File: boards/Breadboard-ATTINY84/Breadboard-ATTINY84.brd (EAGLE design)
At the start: 15.2 x 27.9 mm, 8 parts, among them J1 PINHD-1X7, J2 PINHD-1X7, U1 ATTINY84-20PU

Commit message: Updated breadboard ATTiny84
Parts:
- added D2: LED-0805, SaintGimp:LED-0805
- added R3: 330R, SaintGimp:RESISTOR-0805
- D1: value LED -> LED-0805; device SaintGimp:LED5MM -> SaintGimp:LED-0805
- moved D1 2.84 mm to (8.89, 25.4)
- moved R1 1.90 mm to (8.89, 21.0), flipped to the top, turned to 90 degrees
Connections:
- removed net N$5: J1.5, U1.5
- new net LED: J1.5, R3.1, U1.5
- new net N$1: D2.1, R3.2
- net GND: now also D1.2, D2.2; no longer D1.K
- net N$7: now also D1.1; no longer D1.A
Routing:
- net LED: track 0.00 -> 20.6 mm, vias 0 -> 1
- net GND: track 0.00 -> 4.03 mm, vias 0 -> 1
- net MISO: track 29.1 -> 25.5 mm
- net N$7: track 5.45 -> 2.45 mm
- net N$5: track 2.54 -> 0.00 mm
- net N$1: track 0.00 -> 2.45 mm
- net VCC: track 16.6 -> 19.0 mm, vias 0 -> 1
- net SCK: track 27.0 -> 26.2 mm
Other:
- board text added: "PIN5"
- board text added: "PWR"
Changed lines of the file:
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@@
 <layer number="112" name="tSilk" color="7" fill="1" visible="yes" active="yes"/>
 <layer number="113" name="IDFDebug" color="7" fill="1" visible="yes" active="yes"/>
+<layer number="114" name="FRNTMAAT1" color="7" fill="1" visible="yes" active="yes"/>
+<layer number="115" name="FRNTMAAT2" color="7" fill="1" visible="yes" active="yes"/>
 <layer number="116" name="Patch_BOT" color="9" fill="4" visible="yes" active="yes"/>
+<layer number="117" name="BACKMAAT1" color="7" fill="1" visible="yes" active="yes"/>
 <layer number="118" name="Rect_Pads" color="7" fill="1" visible="no" active="no"/>
+<layer number="119" name="KAP_TEKEN" color="7" fill="1" visible="yes" active="yes"/>
+<layer number="120" name="KAP_MAAT1" color="7" fill="1" visible="yes" active="yes"/>
 <layer number="121" name="_tsilk" color="7" fill="1" visible="yes" active="yes"/>
 <layer number="122" name="_bsilk" color="7" fill="1" visible="yes" active="yes"/>
@@
 <layer number="128" name="_bValues" color="7" fill="1" visible="yes" active="yes"/>
 <layer number="129" name="Mask" color="7" fill="1" visible="yes" active="yes"/>
+<layer number="130" name="SMDSTROOK" color="7" fill="1" visible="yes" active="yes"/>
 <layer number="131" name="tAdjust" color="7" fill="1" visible="no" active="yes"/>
 <layer number="132" name="bAdjust" color="7" fill="1" visible="no" active="yes"/>
@@
 <text x="5.715" y="1.27" size="1.016" layer="122" rot="MR90">v1.1</text>
 <text x="6.985" y="1.27" size="1.016" layer="122" rot="MR90">ATTiny84</text>
+<circle x="5.842" y="19.304" radius="0.359209375" width="0.6096" layer="121"/>
+<text x="7.62" y="24.13" size="0.8128" layer="121" rot="R90">PWR</text>
+<text x="14.605" y="24.13" size="0.8128" layer="121" rot="R90">PIN5</text>
 </plain>
 <attributes>
@@
 </class>
 </classes>
-<designrules name="Saintgimp-OSHPark">
+<designrules name="Saintgimp-OSHPark *">
 <description language="de">&lt;b&gt;EAGLE Design Rules&lt;/b&gt;
 &lt;p&gt;
@@
 <param name="msMicroVia" value="13mil"/>
 <param name="msBlindViaRatio" value="0.5"/>
-<param name="rvPadTop" value="0.4"/>
+<param name="rvPadTop" value="0.35"/>
 <param name="rvPadInner" value="0.25"/>
-<param name="rvPadBottom" value="0.4"/>
+<param name="rvPadBottom" value="0.35"/>
 <param name="rvViaOuter" value="0.25"/>
 <param name="rvViaInner" value="0.25"/>
@@
 <attribute name="NAME" x="10.287" y="16.3195" size="0.8128" layer="26" rot="MR0"/>
 </element>
-<element name="D1" library="SaintGimp" package="LED5MM" value="LED" x="11.43" y="24.13" smashed="yes" rot="R90">
-<attribute name="NAME" x="13.4366" y="20.32" size="0.8128" layer="25" ratio="10"/>
-</element>
-<element name="R1" library="SaintGimp" package="RESISTOR-0805" value="330R" x="8.89" y="19.05" smashed="yes" rot="MR180">
-<attribute name="NAME" x="10.668" y="19.2405" size="0.8128" layer="26" rot="MR180"/>
+<element name="D1" library="SaintGimp" package="LED-0805" value="LED-0805" x="8.89" y="25.4" smashed="yes" rot="R90"/>
+<element name="R1" library="SaintGimp" package="RESISTOR-0805" value="330R" x="8.89" y="20.955" smashed="yes" rot="R90">
+<attribute name="NAME" x="7.8105" y="20.193" size="0.8128" layer="25" rot="R90"/>
 </element>
 <element name="R2" library="SaintGimp" package="RESISTOR-0805" value="10K" x="6.35" y="12.7" smashed="yes" rot="MR90">
@@
 <element name="J1" library="SaintGimp" package="1X07" value="PINHD-1X7" x="1.27" y="8.89" smashed="yes" rot="MR270"/>
 <element name="J2" library="SaintGimp" package="1X07" value="PINHD-1X7" x="13.97" y="8.89" smashed="yes" rot="MR90"/>
+<element name="R3" library="SaintGimp" package="RESISTOR-0805" value="330R" x="12.7" y="20.955" smashed="yes" rot="R90">
+<attribute name="NAME" x="11.6205" y="20.193" size="0.8128" layer="25" rot="R90"/>
+</element>
+<element name="D2" library="SaintGimp" package="LED-0805" value="LED-0805" x="12.7" y="25.4" smashed="yes" rot="R90"/>
 </elements>
 <signals>
@@
 <contactref element="ISP1" pad="6"/>
 <contactref element="C1" pad="1"/>
-<contactref element="D1" pad="K"/>
+<contactref element="D1" pad="2"/>
 <contactref element="U1" pad="14"/>
 <contactref element="J2" pad="7"/>
+<via x="10.795" y="26.67" extent="1-16" drill="0.5"/>
+<wire x1="8.89" y1="26.4" x2="9.16" y2="26.67" width="0.254" layer="1"/>
+<wire x1="9.16" y1="26.67" x2="10.795" y2="26.67" width="0.254" layer="1"/>
+<contactref element="D2" pad="2"/>
+<wire x1="12.7" y1="26.4" x2="12.43" y2="26.67" width="0.254" layer="1"/>
+<wire x1="12.43" y1="26.67" x2="10.795" y2="26.67" width="0.254" layer="1"/>
 </signal>
 <signal name="MISO">
@@
 <contactref element="U1" pad="8"/>
 <contactref element="J2" pad="1"/>
-<wire x1="5.08" y1="21.59" x2="5.08" y2="20.955" width="0.254" layer="1"/>
-<wire x1="5.08" y1="20.955" x2="6.35" y2="22.225" width="0.254" layer="1"/>
-<wire x1="6.35" y1="22.225" x2="8.255" y2="22.225" width="0.254" layer="1"/>
-<wire x1="8.255" y1="22.225" x2="9.525" y2="20.955" width="0.254" layer="1"/>
-<wire x1="9.525" y1="20.955" x2="9.525" y2="3.175" width="0.254" layer="1"/>
-<wire x1="9.525" y1="3.175" x2="11.43" y2="1.27" width="0.254" layer="1"/>
 <wire x1="11.43" y1="1.27" x2="13.97" y2="1.27" width="0.254" layer="1"/>
+<wire x1="5.08" y1="21.59" x2="5.715" y2="20.955" width="0.254" layer="1"/>
+<wire x1="5.715" y1="20.955" x2="5.715" y2="6.985" width="0.254" layer="1"/>
+<wire x1="5.715" y1="6.985" x2="11.43" y2="1.27" width="0.254" layer="1"/>
 </signal>
 <signal name="SCK">
@@
 <contactref element="U1" pad="9"/>
 <contactref element="J2" pad="2"/>
-<wire x1="10.16" y1="21.59" x2="10.16" y2="5.08" width="0.254" layer="1"/>
-<wire x1="10.16" y1="5.08" x2="11.43" y2="3.81" width="0.254" layer="1"/>
 <wire x1="13.97" y1="3.81" x2="11.43" y2="3.81" width="0.254" layer="1"/>
-<wire x1="10.16" y1="21.59" x2="7.62" y2="24.13" width="0.254" layer="1"/>
-<wire x1="7.62" y1="24.13" x2="5.08" y2="24.13" width="0.254" layer="1"/>
+<wire x1="5.08" y1="24.13" x2="6.35" y2="22.86" width="0.254" layer="1"/>
+<wire x1="6.35" y1="22.86" x2="6.35" y2="7.62" width="0.254" layer="1"/>
+<wire x1="11.43" y1="3.81" x2="10.16" y2="3.81" width="0.254" layer="1"/>
+<wire x1="10.16" y1="3.81" x2="6.35" y2="7.62" width="0.254" layer="1"/>
 </signal>
 <signal name="RST">
@@
 <wire x1="5.985" y1="14.065" x2="5.985" y2="16.51" width="0.254" layer="16"/>
 <wire x1="5.985" y1="16.51" x2="3.81" y2="16.51" width="0.254" layer="16"/>
-<wire x1="5.985" y1="16.51" x2="5.985" y2="17.145" width="0.254" layer="16"/>
-<wire x1="5.985" y1="17.145" x2="7.89" y2="19.05" width="0.254" layer="16"/>
 <wire x1="2.54" y1="21.59" x2="2.54" y2="17.78" width="0.254" layer="1"/>
 <wire x1="2.54" y1="17.78" x2="3.81" y2="16.51" width="0.254" layer="1"/>
 <wire x1="3.81" y1="16.51" x2="1.27" y2="16.51" width="0.254" layer="1"/>
+<wire x1="5.985" y1="16.51" x2="5.985" y2="17.415" width="0.254" layer="16"/>
+<wire x1="5.985" y1="17.415" x2="6.35" y2="17.78" width="0.254" layer="16"/>
+<wire x1="6.35" y1="17.78" x2="8.255" y2="17.78" width="0.254" layer="16"/>
+<wire x1="8.255" y1="17.78" x2="8.89" y2="18.415" width="0.254" layer="16"/>
+<via x="8.89" y="18.415" extent="1-16" drill="0.5"/>
+<wire x1="8.89" y1="18.415" x2="8.89" y2="19.955" width="0.254" layer="1"/>
 </signal>
 <signal name="MOSI">
@@
 </signal>
 <signal name="N$7">
-<contactref element="D1" pad="A"/>
+<contactref element="D1" pad="1"/>
 <contactref element="R1" pad="2"/>
-<wire x1="9.89" y1="20.05" x2="9.89" y2="19.05" width="0.254" layer="16"/>
-<wire x1="11.43" y1="22.86" x2="11.43" y2="20.59" width="0.254" layer="16"/>
-<wire x1="11.43" y1="20.59" x2="9.89" y2="19.05" width="0.254" layer="16"/>
+<wire x1="8.89" y1="24.4" x2="8.89" y2="21.955" width="0.254" layer="1"/>
 </signal>
 <signal name="N$2">
@@
 <wire x1="3.81" y1="11.43" x2="1.27" y2="11.43" width="0.254" layer="1"/>
 </signal>
-<signal name="N$5">
+<signal name="LED">
 <contactref element="U1" pad="5"/>
 <contactref element="J1" pad="5"/>
 <wire x1="1.27" y1="6.35" x2="3.81" y2="6.35" width="0.254" layer="1"/>
+<contactref element="R3" pad="1"/>
+<wire x1="3.81" y1="6.35" x2="5.08" y2="6.35" width="0.254" layer="16"/>
+<wire x1="5.08" y1="6.35" x2="7.62" y2="8.89" width="0.254" layer="16"/>
+<via x="7.62" y="8.89" extent="1-16" drill="0.5"/>
+<wire x1="7.62" y1="8.89" x2="7.62" y2="14.875" width="0.254" layer="1"/>
+<wire x1="7.62" y1="14.875" x2="12.7" y2="19.955" width="0.254" layer="1"/>
 </signal>
 <signal name="N$6">
@@
 <wire x1="13.97" y1="13.97" x2="11.43" y2="13.97" width="0.254" layer="1"/>
 </signal>
+<signal name="N$1">
+<contactref element="D2" pad="1"/>
+<contactref element="R3" pad="2"/>
+<wire x1="12.7" y1="24.4" x2="12.7" y2="21.955" width="0.254" layer="1"/>
+</signal>
 </signals>

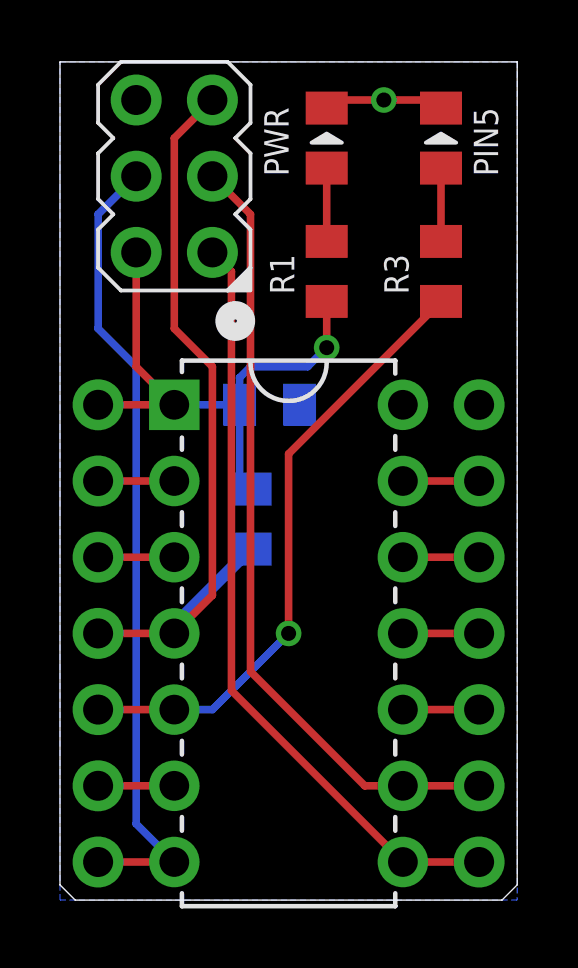
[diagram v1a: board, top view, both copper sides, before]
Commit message: Updated breadboard ATMega328
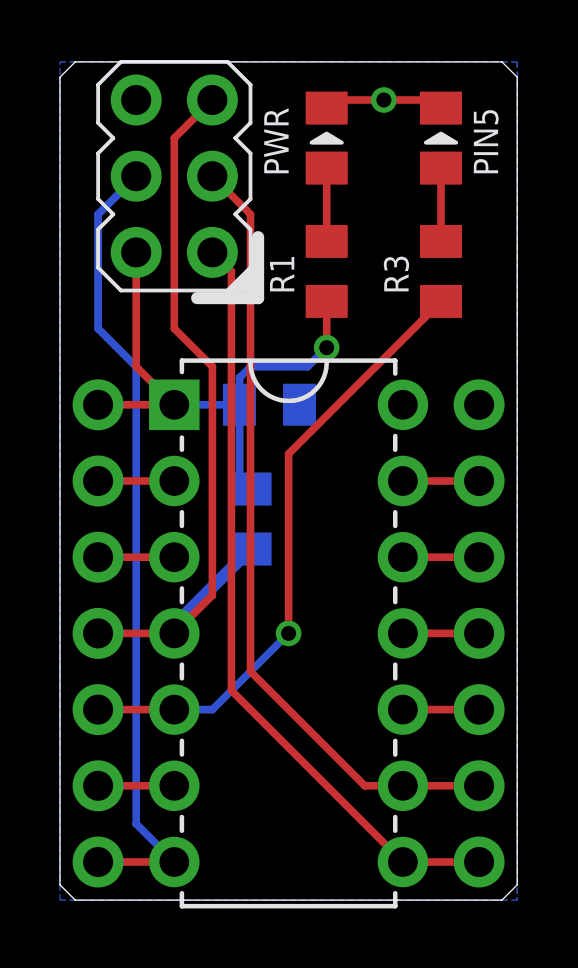
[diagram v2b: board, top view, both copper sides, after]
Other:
- outline, holes or cut-outs redrawn
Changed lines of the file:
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@@
 <setting verticaltext="up"/>
 </settings>
-<grid distance="0.05" unitdist="inch" unit="inch" style="lines" multiple="1" display="no" altdistance="0.025" altunitdist="inch" altunit="inch"/>
+<grid distance="0.05" unitdist="inch" unit="inch" style="lines" multiple="1" display="no" altdistance="0.01" altunitdist="inch" altunit="inch"/>
 <layers>
 <layer number="1" name="Top" color="4" fill="1" visible="yes" active="yes"/>
@@
 <board>
 <plain>
-<wire x1="0" y1="0.508" x2="0" y2="27.94" width="0" layer="20"/>
-<wire x1="0" y1="27.94" x2="15.24" y2="27.94" width="0" layer="20"/>
-<wire x1="15.24" y1="27.94" x2="15.24" y2="0.508" width="0" layer="20"/>
+<wire x1="0" y1="0.508" x2="0" y2="27.432" width="0" layer="20"/>
+<wire x1="0" y1="27.432" x2="0.508" y2="27.94" width="0" layer="20"/>
+<wire x1="0.508" y1="27.94" x2="14.732" y2="27.94" width="0" layer="20"/>
+<wire x1="14.732" y1="27.94" x2="15.24" y2="27.432" width="0" layer="20"/>
+<wire x1="15.24" y1="27.432" x2="15.24" y2="0.508" width="0" layer="20"/>
 <wire x1="15.24" y1="0.508" x2="14.732" y2="0" width="0" layer="20"/>
 <wire x1="14.732" y1="0" x2="0.508" y2="0" width="0" layer="20"/>
@@
 <text x="5.715" y="1.27" size="1.016" layer="122" rot="MR90">v1.1</text>
 <text x="6.985" y="1.27" size="1.016" layer="122" rot="MR90">ATTiny84</text>
-<circle x="5.842" y="19.304" radius="0.359209375" width="0.6096" layer="121"/>
 <text x="7.62" y="24.13" size="0.8128" layer="121" rot="R90">PWR</text>
 <text x="14.605" y="24.13" size="0.8128" layer="121" rot="R90">PIN5</text>
+<wire x1="4.572" y1="20.066" x2="6.604" y2="20.066" width="0.4064" layer="121"/>
+<wire x1="6.604" y1="20.066" x2="6.604" y2="22.098" width="0.4064" layer="121"/>
 </plain>
 <attributes>
